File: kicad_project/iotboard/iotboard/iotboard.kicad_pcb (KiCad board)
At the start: 2 copper layers, 43 parts, among them J1 Conn_01x02, J2 USB_B_Micro, J3 Conn_01x12, J4 Conn_01x16, Q1 mmbt2222, Q2 mmbt2222, SW1 SW_Push, SW2 SW_Push, U1 AP2127K-3.3, U2 CP2102N-A01-GQFN24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

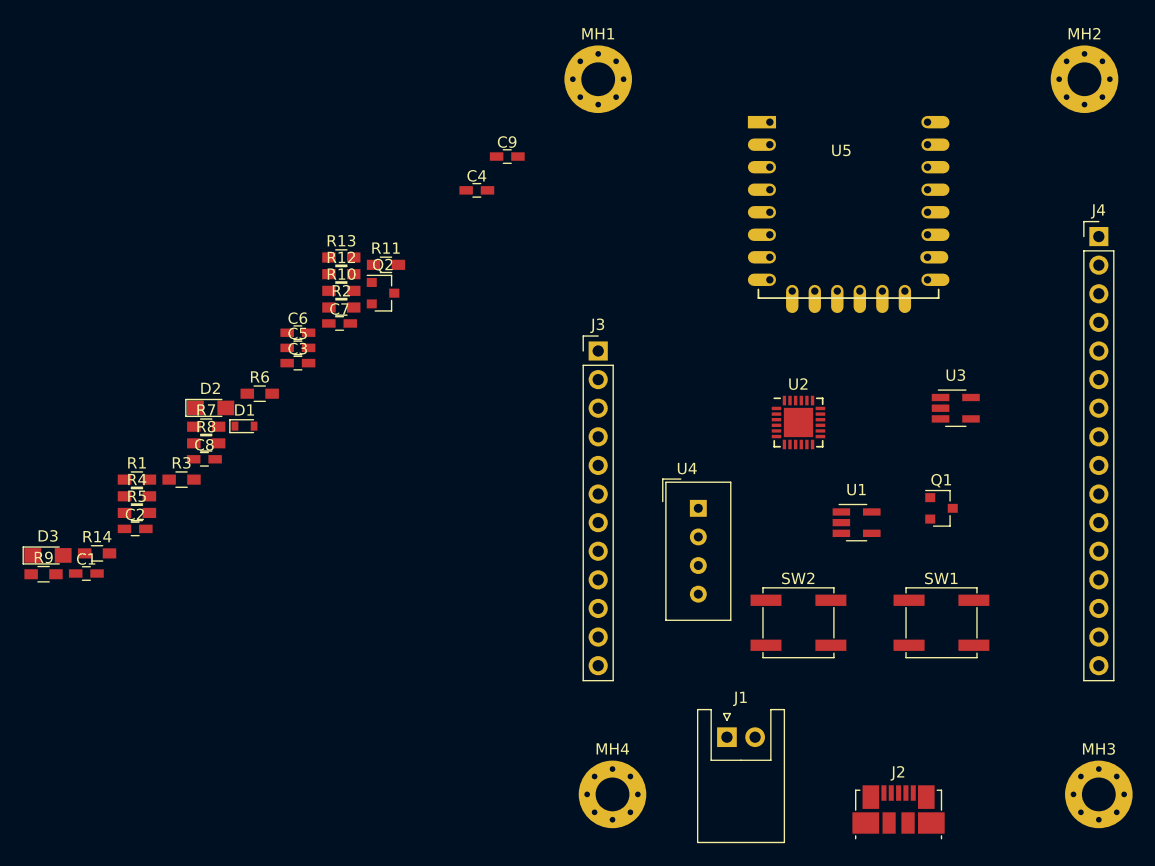
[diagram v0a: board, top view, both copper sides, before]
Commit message: added KiCAD PCB y project
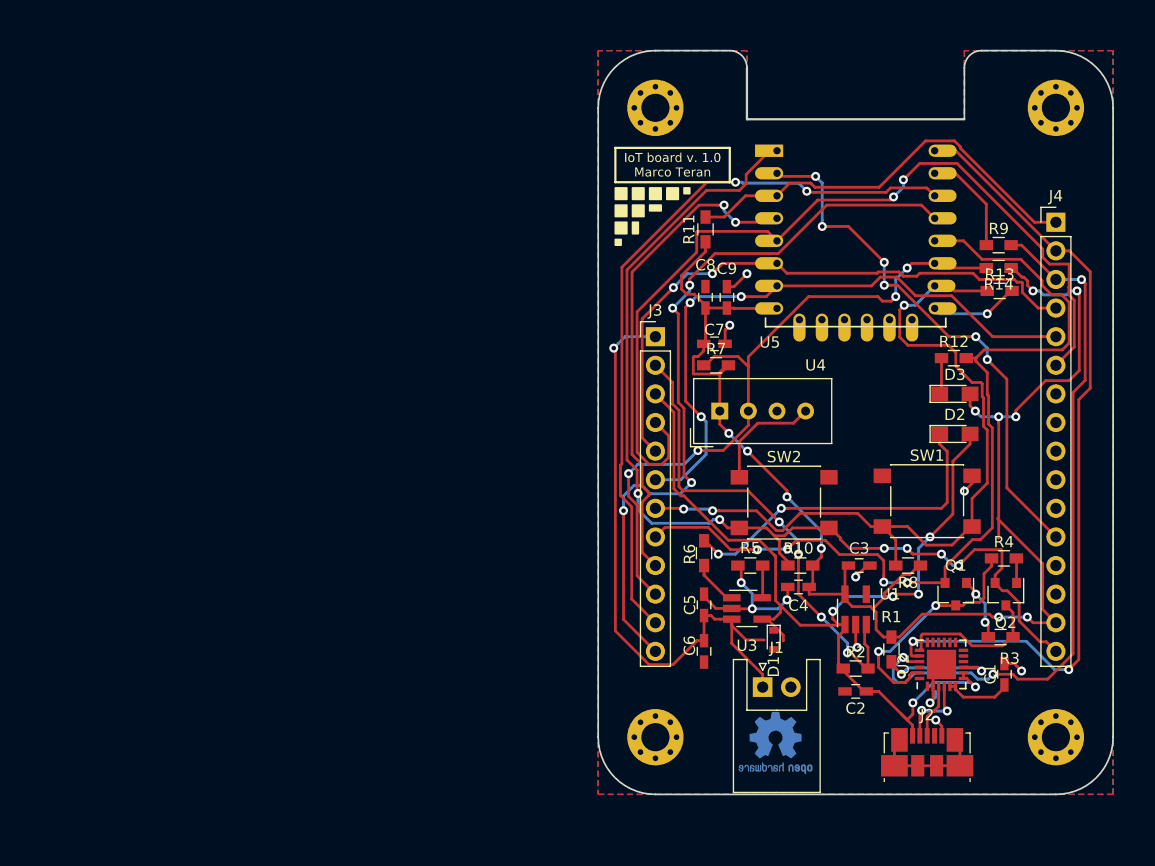
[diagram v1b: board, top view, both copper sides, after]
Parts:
- added G***: logousasmall, mycustomfootprints:logousasmall, B.Cu at (142.2, 103.1)
- added REF***: KiCad-Logo2_6mm_SilkScreen, Symbols:KiCad-Logo2_6mm_SilkScreen, B.Cu at (133.6, 124.0)
- added REF***: OSHW-Logo2_7.3x6mm_Copper, Symbols:OSHW-Logo2_7.3x6mm_Copper, B.Cu at (135.1, 135.1)
- MH1, MH2, MH3, MH4: footprint Mounting_Holes:MountingHole_3mm_Pad_Via -> Mounting_Holes:MountingHole_2.5mm_Pad_Via
- SW1, SW2: footprint Buttons_Switches_SMD:SW_SPST_EVPBF -> Buttons_Switches_SMD:SW_SPST_PTS645
- moved R9 89.7 mm to (154.9, 90.9)
- moved R14 84.0 mm to (154.9, 93.0), turned to 180 degrees
- moved C1 82.0 mm to (155.4, 129.0), turned to 90 degrees
- moved D3 81.8 mm to (151.1, 104.1)
- moved R4 77.2 mm to (155.4, 118.7)
- moved R3 74.1 mm to (155.1, 125.7), turned to 180 degrees
- moved R1 68.7 mm to (145.4, 126.8), turned to 270 degrees
- moved D2 66.1 mm to (151.1, 107.7)
- moved C2 65.6 mm to (142.2, 130.6), turned to 180 degrees
- moved R8 63.3 mm to (146.9, 119.4), turned to 180 degrees
- moved Q2 61.4 mm to (155.6, 121.9), turned to 270 degrees
- moved R13 58.5 mm to (155.0, 95.0)
- moved R2 55.8 mm to (142.2, 128.5)
- moved R12 54.9 mm to (151.0, 101.0)
- moved R5 54.7 mm to (132.9, 119.4), turned to 180 degrees
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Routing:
- net +3V3: track 0.00 -> 134.4 mm, vias 0 -> 11
- net RST: track 0.00 -> 91.3 mm, vias 0 -> 6
- net VBUS: track 0.00 -> 87.3 mm, vias 0 -> 6
- net GPIO0: track 0.00 -> 80.4 mm, vias 0 -> 4
- net GPIO14_SCK: track 0.00 -> 79.5 mm, vias 0 -> 2
- net TXD: track 0.00 -> 71.3 mm, vias 0 -> 2
- net GPIO15: track 0.00 -> 69.8 mm, vias 0 -> 3
- net GPIO4_SDA: track 0.00 -> 66.5 mm, vias 0 -> 4
- net GPIO5_SCL: track 0.00 -> 64.6 mm, vias 0 -> 3
- net RXD: track 0.00 -> 63.1 mm, vias 0 -> 3
- net GPIO2: track 0.00 -> 60.8 mm, vias 0 -> 4
- net GPIO13_MOSI: track 0.00 -> 55.4 mm, vias 0 -> 3
- net +BATT: track 0.00 -> 55.3 mm, vias 0 -> 1
- net GND: track 0.00 -> 54.3 mm, vias 0 -> 12
- net GPIO12_MISO: track 0.00 -> 53.5 mm, vias 0 -> 2
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- added copper zone on B.Cu, net GND
- added copper zone on F.Cu, net GND
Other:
- board outline added: 45.7 x 66 mm
- board text added: "General purpose IoT board Temperature and humidity sensor"
- board text added: "IoT board v. 1.0 Marco Teran"
